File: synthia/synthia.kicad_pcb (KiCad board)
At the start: 2 copper layers, 300 x 271.1 mm, 205 parts, among them J1 MJ-63022B, J2 SJ3-35083C-TR, J3 PJ-007, J4 SDS-50J, Q1 IRF9540N, U1 TLV272IP, U2 STM32H750ZBT6, U3 LD1117V33, U4 PVA1EEH31.2NV2, U5 PVA1EEH31.2NV2

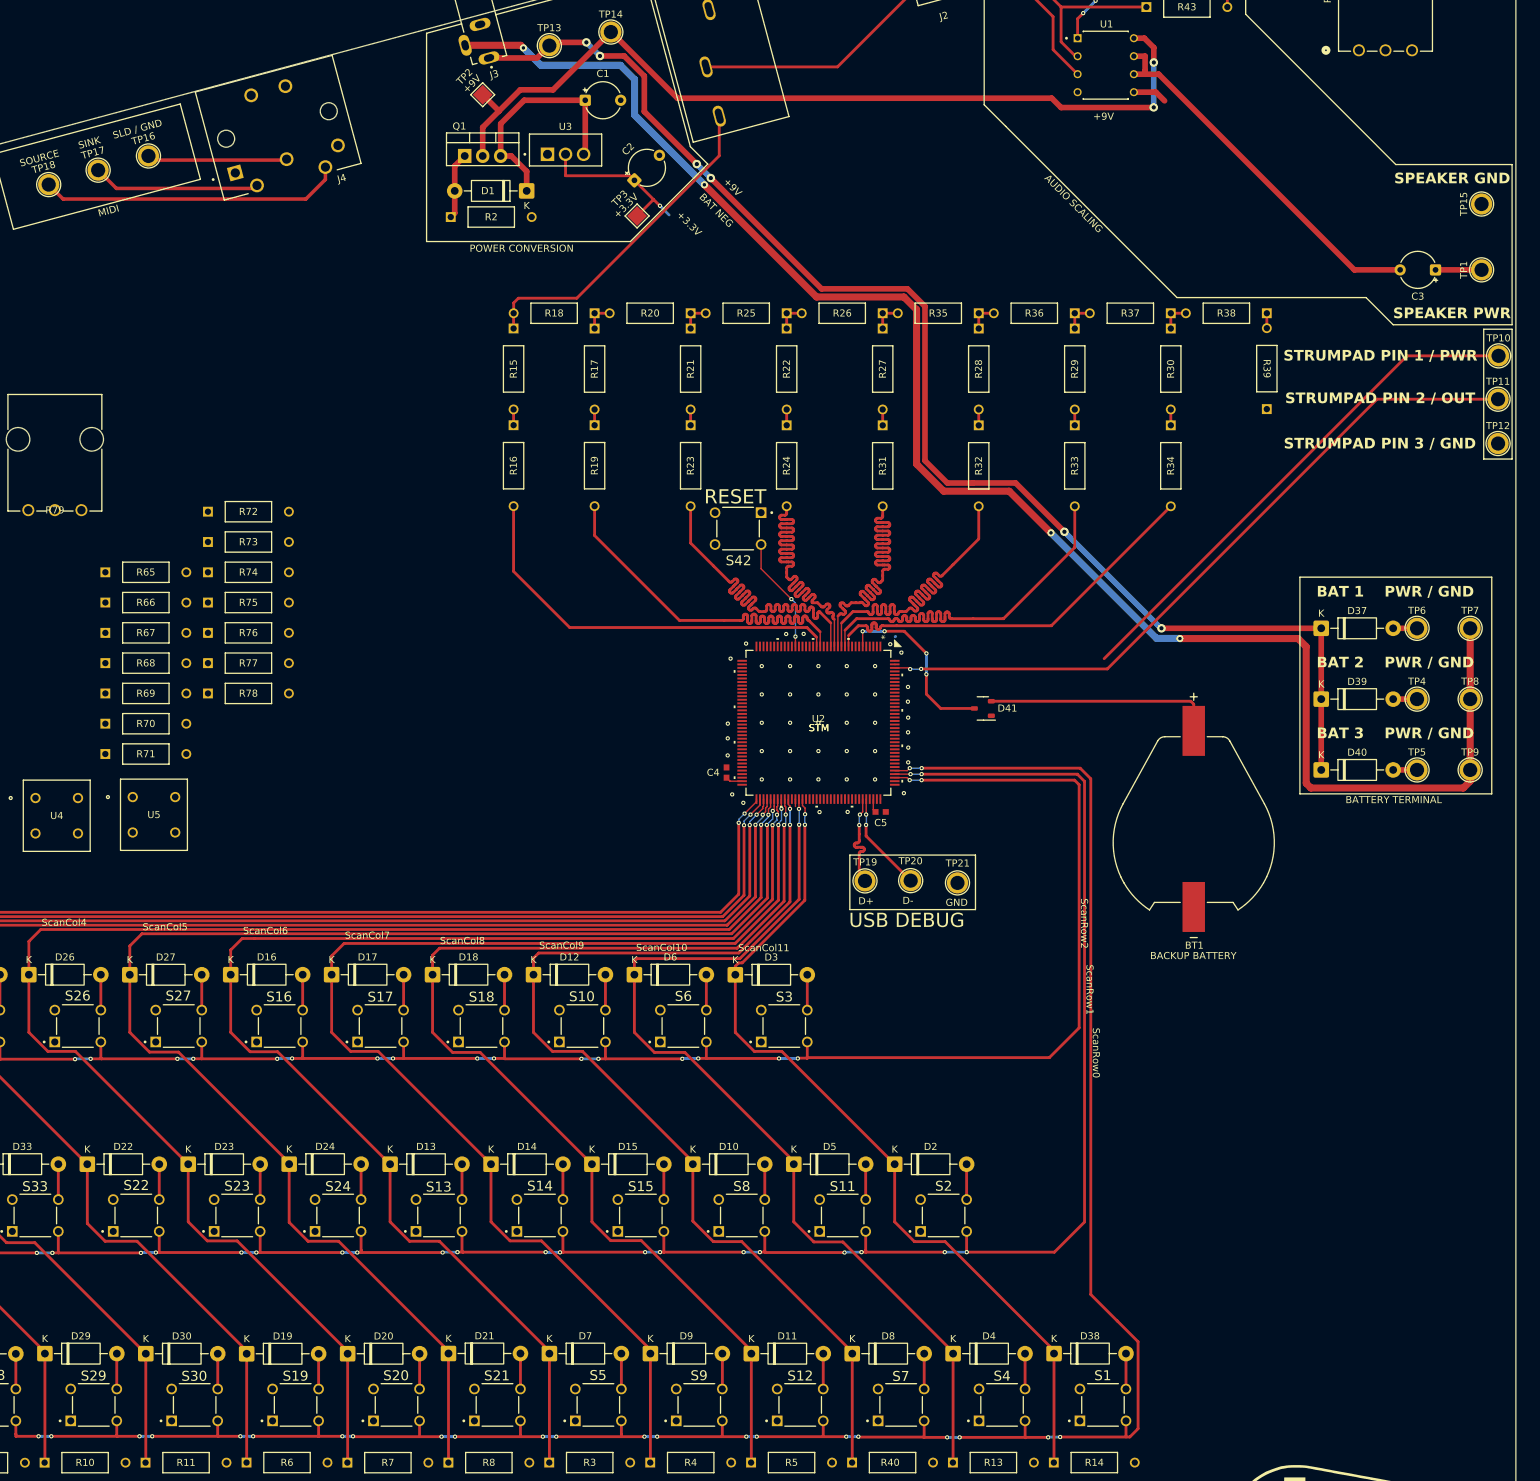
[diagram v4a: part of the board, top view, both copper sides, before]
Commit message: Updated schematic now routed on the PCB, everything should be prepped for next step
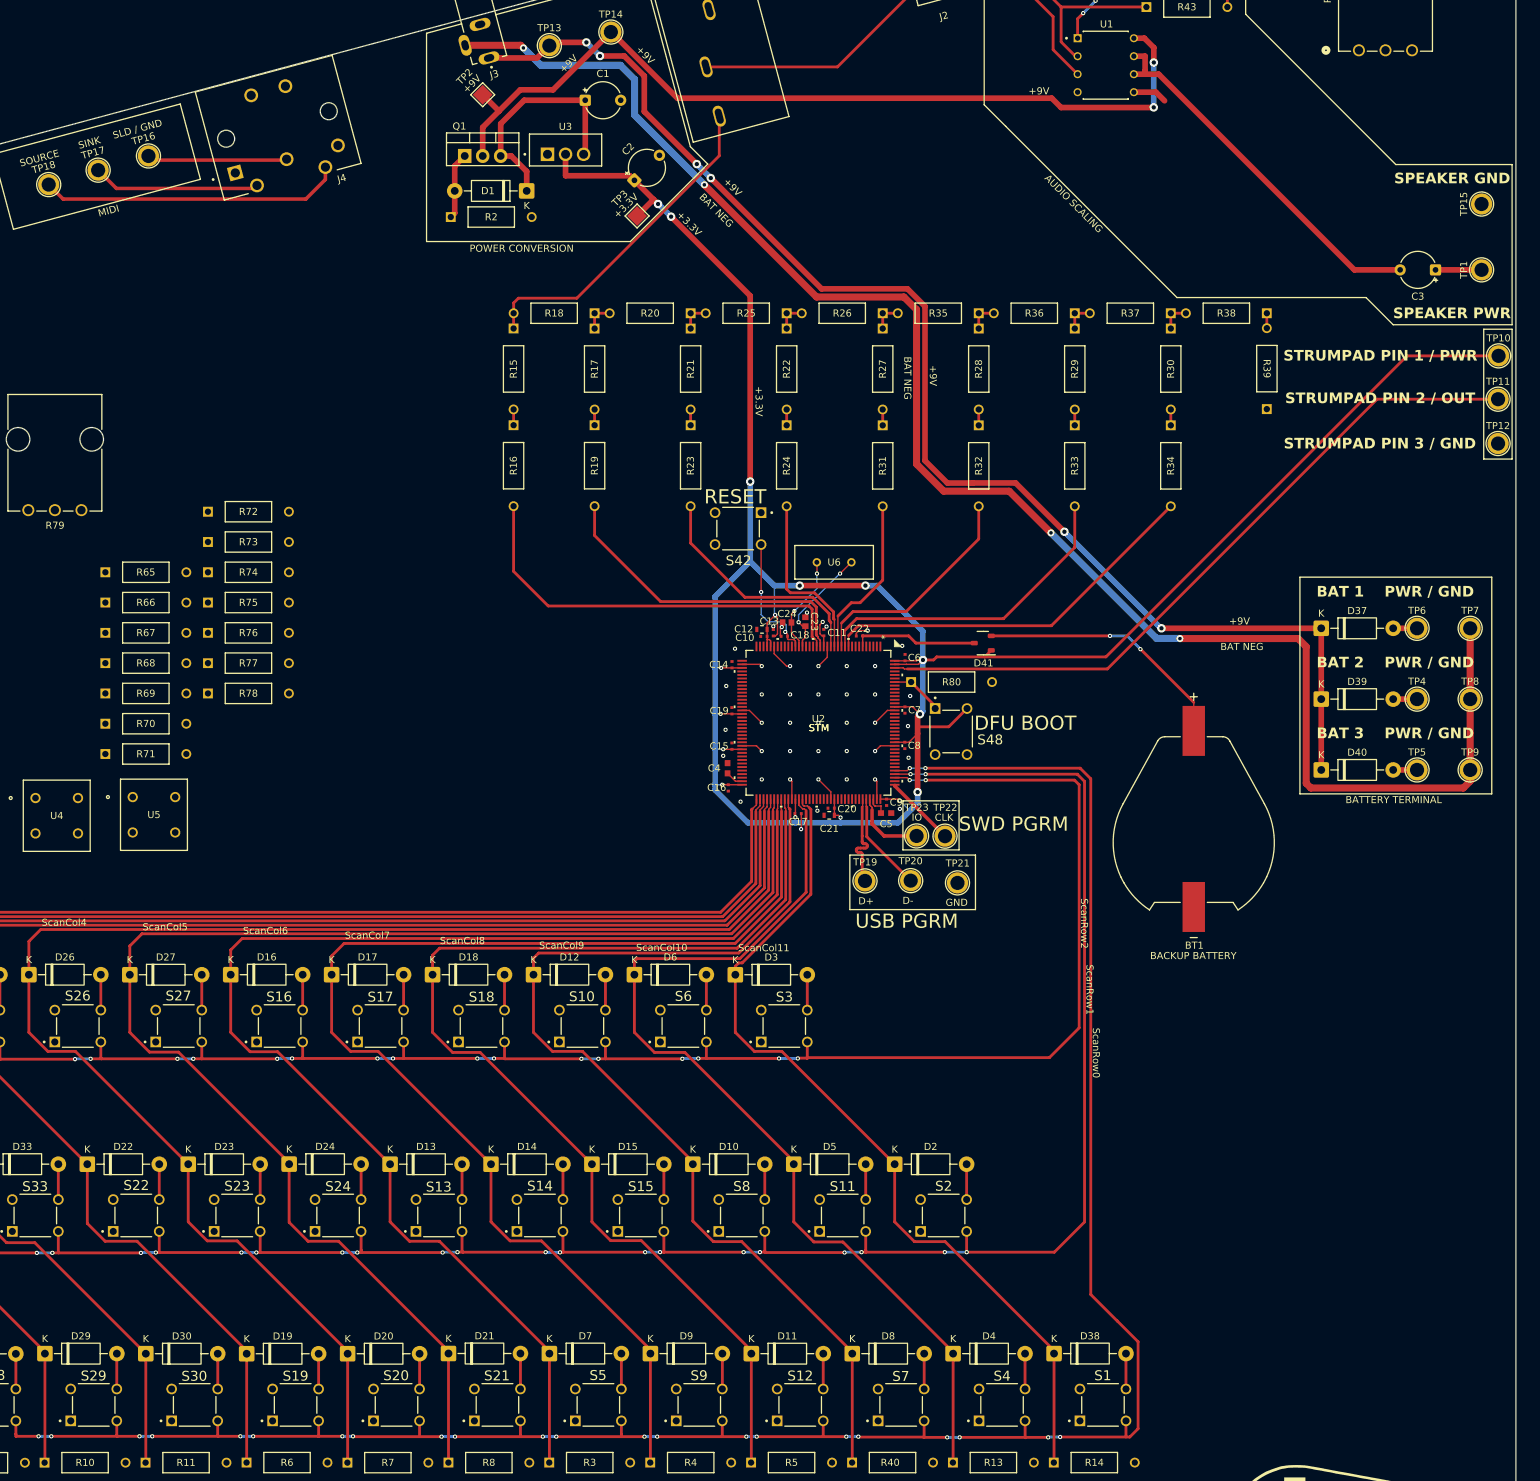
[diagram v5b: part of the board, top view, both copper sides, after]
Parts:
- added C10: CL05B104KP5NNNC, Synthia_footprint_library:CAP_CL05_SAM-L, F.Cu at (289.4, 210.0)
- added C11: CL05B104KP5NNNC, Synthia_footprint_library:CAP_CL05_SAM-L, F.Cu at (297.9, 209.5)
- added C12: CL10B105KA8NNNC, Synthia_footprint_library:CAP_CL10_SAM-L, F.Cu at (289.1, 209.0)
- added C13: CL05B104KP5NNNC, Synthia_footprint_library:CAP_CL05_SAM-L, F.Cu at (290.8, 209.5)
- added C14: CL05B104KP5NNNC, Synthia_footprint_library:CAP_CL05_SAM-L, F.Cu at (284.9, 214.0)
- added C15: CL05B104KP5NNNC, Synthia_footprint_library:CAP_CL05_SAM-L, F.Cu at (284.9, 225.5)
- added C16: CL05B104KP5NNNC, Synthia_footprint_library:CAP_CL05_SAM-L, F.Cu at (284.4, 231.4)
- added C17: CL05B104KP5NNNC, Synthia_footprint_library:CAP_CL05_SAM-L, F.Cu at (294.2, 235.0)
- added C18: CL05B104KP5NNNC, Synthia_footprint_library:CAP_CL05_SAM-L, F.Cu at (292.3, 210.0)
- added C19: CL05B104KP5NNNC, Synthia_footprint_library:CAP_CL05_SAM-L, F.Cu at (284.9, 220.5)
- added C20: CL05B104KP5NNNC, Synthia_footprint_library:CAP_CL05_SAM-L, F.Cu at (298.9, 234.3)
- added C21: CL10B105KA8NNNC, Synthia_footprint_library:CAP_CL10_SAM-L, F.Cu at (298.6, 235.3)
- added C22: CL05B104KP5NNNC, Synthia_footprint_library:CAP_CL05_SAM-L, F.Cu at (302.9, 209.9)
- added C23: C0603C330J5GACTU, Synthia_footprint_library:CAPC17595_87N_KEM-L, F.Cu at (295.3, 207.9)
- added C24: C0603C330J5GACTU, Synthia_footprint_library:CAPC17595_87N_KEM-L, F.Cu at (292.7, 208.0)
- added C6: CL05B104KP5NNNC, Synthia_footprint_library:CAP_CL05_SAM-L, F.Cu at (309.4, 213.0)
- added C7: CL05B104KP5NNNC, Synthia_footprint_library:CAP_CL05_SAM-L, F.Cu at (309.3, 220.4)
- added C8: CL05B104KP5NNNC, Synthia_footprint_library:CAP_CL05_SAM-L, F.Cu at (309.3, 225.4)
- added C9: CL05B104KP5NNNC, Synthia_footprint_library:CAP_CL05_SAM-L, F.Cu at (306.7, 233.4)
- added R80: 100k, Synthia_footprint_library:STA_CF14_STP, F.Cu at (310.2, 216.4)
- added S48: DFU BOOT, Synthia_footprint_library:SW_TL1105BF160Q, F.Cu at (315.9, 223.4)
- added TP22: SWCLK, TestPoint:TestPoint_Plated_Hole_D2.0mm, F.Cu at (315.0, 238.2)
- added TP23: SWDIO, TestPoint:TestPoint_Plated_Hole_D2.0mm, F.Cu at (311.0, 238.2)
- added U6: ATS08A-E, Synthia_footprint_library:ATS08A-E_CTS, F.Cu at (301.8, 199.5)
- D41: value BAS70-04 -> BAS70-05
- moved D41 9.23 mm to (321.5, 212.0)
- moved C5 0.79 mm to (306.7, 234.9)
- moved C4 0.63 mm to (284.3, 228.6)
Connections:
- J3 pad 2: GND -> unconnected-(J3-Pad2)
- U2 pad 105: unconnected-(U2B-PA13-Pad105) -> Net-(U2B-PA13)
- U2 pad 109: unconnected-(U2B-PA14-Pad109) -> Net-(U2B-PA14)
- U2 pad 138: +3.3V -> Net-(U2B-BOOT0)
- U2 pad 23: unconnected-(U2A-PH0-OSC_IN-Pad23) -> Net-(U2A-PH0-OSC_IN)
- U2 pad 24: unconnected-(U2A-PH1-OSC_OUT-Pad24) -> Net-(U2A-PH1-OSC_OUT)
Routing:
- net +3.3V: track 98.0 -> 365.8 mm, vias 1 -> 17
- net GND: track 0.00 -> 40.9 mm, vias 45 -> 42
- net /DAC_schematic/DAC3: track 56.7 -> 23.1 mm
- net /DAC_schematic/DAC4: track 56.7 -> 24.6 mm
- net /DAC_schematic/DAC2: track 56.8 -> 32.2 mm
- net /DAC_schematic/DAC5: track 56.7 -> 33.6 mm
- net Net-(U2A-PH0-OSC_IN): track 0.00 -> 15.8 mm, vias 0 -> 2
- net Net-(U2A-PH1-OSC_OUT): track 0.00 -> 13.8 mm, vias 0 -> 2
- net /DAC_schematic/DAC1: track 56.9 -> 45.4 mm
- net /DAC_schematic/DAC6: track 56.9 -> 45.4 mm
- net Net-(U2B-PA13): track 0.00 -> 10.6 mm
- net Net-(U2B-PA14): track 0.00 -> 10.1 mm
- net Net-(D41-C): track 25.8 -> 17.7 mm, vias 4 -> 0
- net Net-(U2B-BOOT0): track 0.00 -> 7.45 mm
- net Net-(BT1-PadP): track 32.5 -> 36.5 mm, vias 0 -> 2
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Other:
- board text added: "CLK"
- board text added: "DFU BOOT"
- board text added: "IO"
- board text added: "SWD PGRM"
- board text added: "USB PGRM"
- board text removed: "USB DEBUG"

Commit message: slight tweak, previous commit still applies\
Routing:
- net GND: vias 42 -> 43
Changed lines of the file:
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@@
+	)
+	(via
+		(at 288.22 209.9)
+		(size 0.6)
+		(drill 0.3)
+		(layers "F.Cu" "B.Cu")
+		(free yes)
+		(net "GND")
 	)
 	(via

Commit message: Cosmetic changes to PCB made
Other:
- board text added: "CRYSTAL"
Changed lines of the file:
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@@
+		)
+	)
+	(gr_text "CRYSTAL\n"
+		(at 292.821515 196.976917 0)
+		(layer "F.SilkS")
+		(effects
+			(font
+				(size 2 2)
+				(thickness 0.3)
+			)
+			(justify left bottom)
 		)
 	)

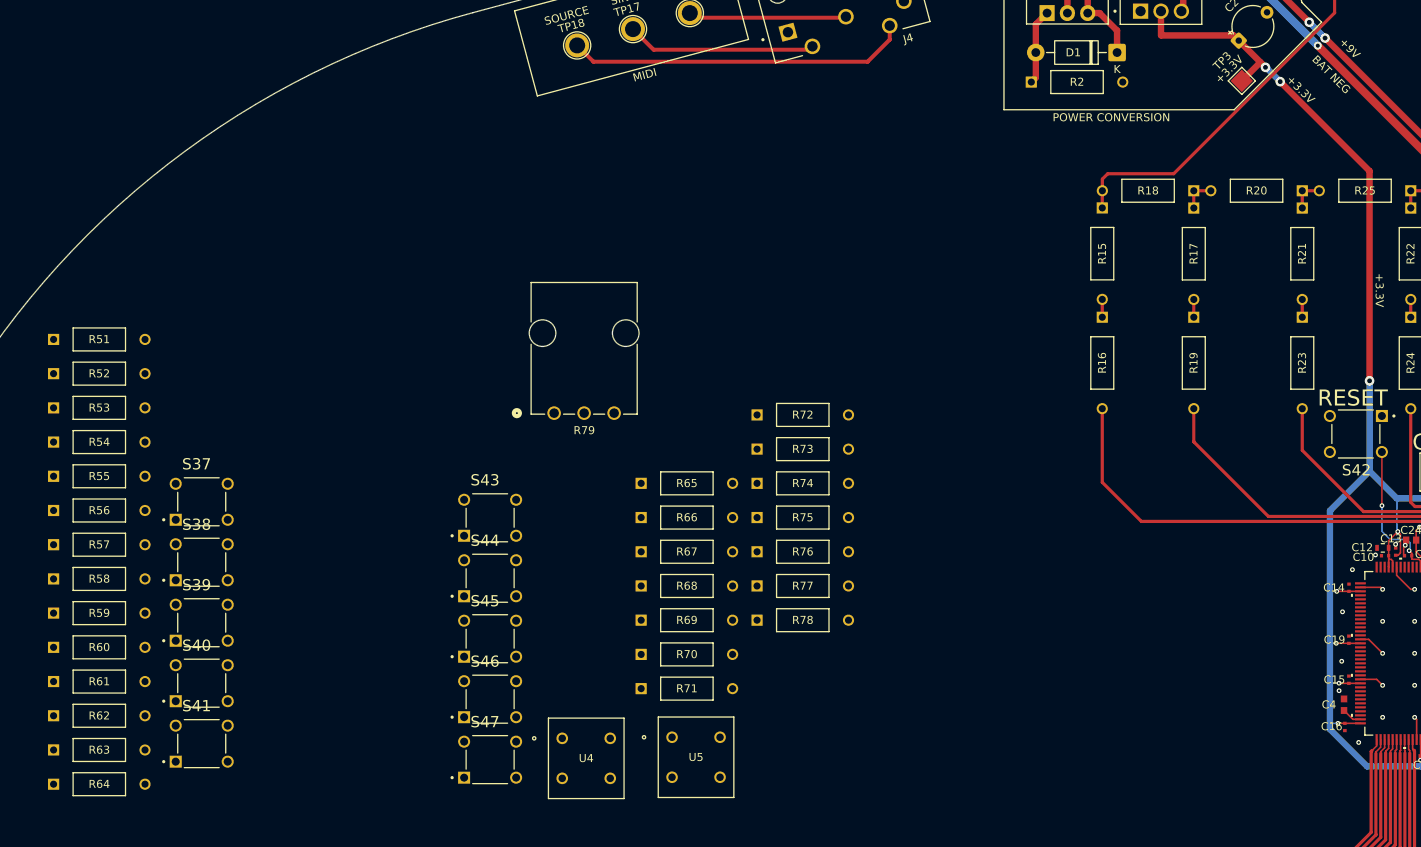
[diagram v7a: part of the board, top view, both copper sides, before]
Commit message: Organized Font and Rhythm button matrices and associated switches. Not in their final location so power and IO is not routed for them yet
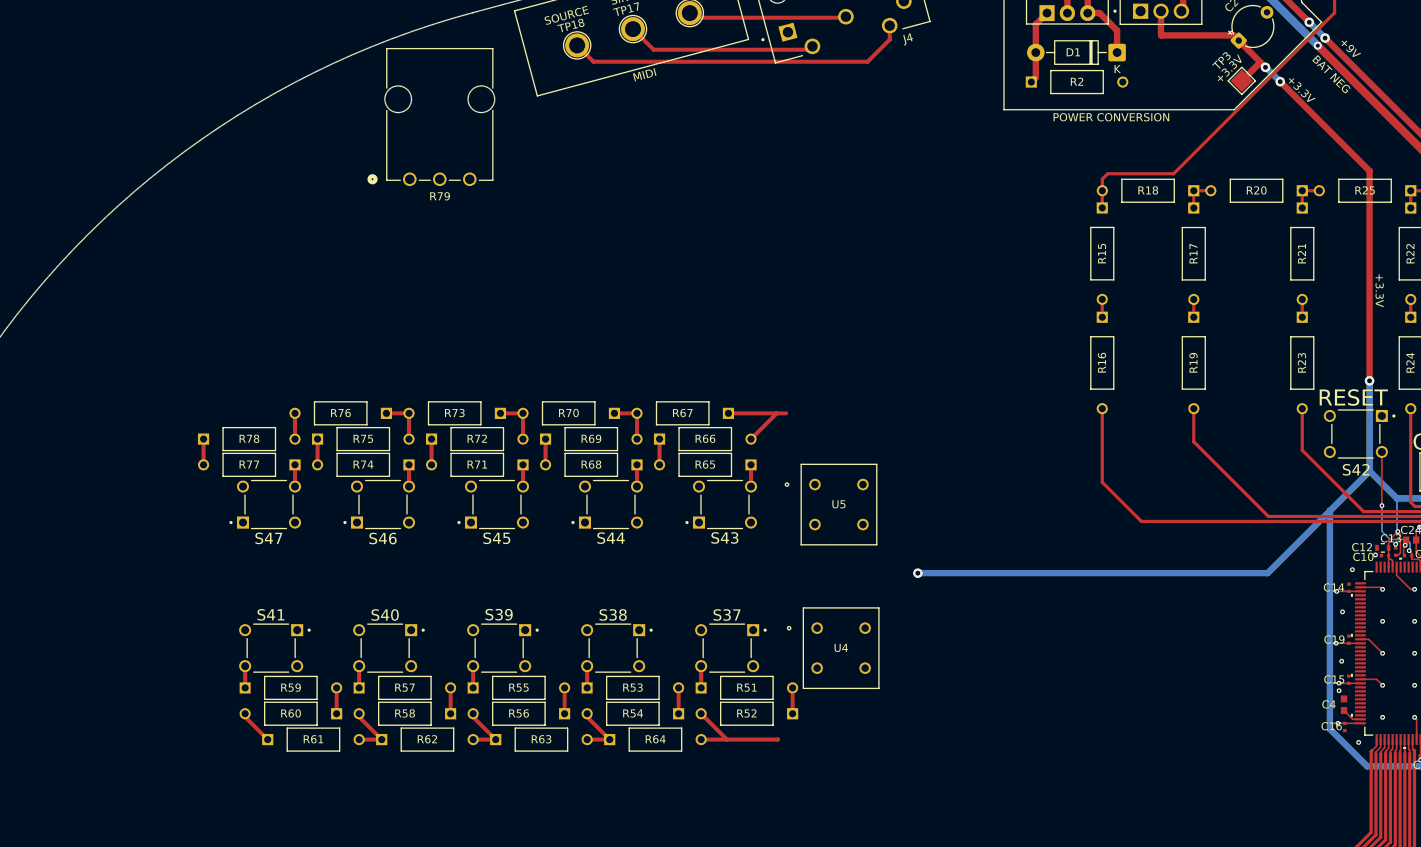
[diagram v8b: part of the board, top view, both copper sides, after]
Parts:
- moved R52 101.7 mm to (215.4, 229.8), turned to 180 degrees
- moved R51 91.9 mm to (203.9, 226.5)
- moved R54 85.2 mm to (201.1, 229.8), turned to 180 degrees
- moved R53 75.3 mm to (189.7, 226.5)
- moved R78 72.8 mm to (141.7, 195.4)
- moved R64 69.7 mm to (192.5, 233.0)
- moved R56 68.7 mm to (186.9, 229.8), turned to 180 degrees
- moved S37 68.2 mm to (207.2, 221.6), turned to 180 degrees
- moved R77 59.7 mm to (153.2, 198.6), turned to 180 degrees
- moved R55 58.7 mm to (175.4, 226.5)
- moved R75 55.8 mm to (156.0, 195.4)
- moved R63 55.3 mm to (178.2, 233.0)
- moved S38 52.5 mm to (192.9, 221.6), turned to 180 degrees
- moved R58 52.4 mm to (172.6, 229.8), turned to 180 degrees
- moved R76 49.5 mm to (164.6, 192.2), turned to 180 degrees
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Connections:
- U5 pad 1: +3.3V -> unconnected-(U5-Pad1)
- U5 pad 2: unconnected-(U5-Pad2) -> +3.3V
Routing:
- net +3.3V: track 365.8 -> 420.6 mm, vias 17 -> 18
- net Net-(R52-Pad2): track 0.00 -> 14.2 mm
- net Net-(R66-Pad2): track 0.00 -> 11.8 mm
- net Net-(R58-Pad2): track 0.00 -> 7.22 mm
- net Net-(R56-Pad2): track 0.00 -> 7.22 mm
- net Net-(R54-Pad2): track 0.00 -> 7.22 mm
- net Net-(R73-Pad2): track 0.00 -> 6.04 mm
- net Net-(R70-Pad2): track 0.00 -> 6.04 mm
- net Net-(R67-Pad2): track 0.00 -> 6.04 mm
- net Net-(R60-Pad2): track 0.00 -> 4.40 mm
- net Net-(R59-Pad2): track 0.00 -> 3.23 mm
- net Net-(R57-Pad2): track 0.00 -> 3.23 mm
- net Net-(R55-Pad2): track 0.00 -> 3.23 mm
- net Net-(R53-Pad2): track 0.00 -> 3.23 mm
- net Net-(R51-Pad2): track 0.00 -> 3.23 mm
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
